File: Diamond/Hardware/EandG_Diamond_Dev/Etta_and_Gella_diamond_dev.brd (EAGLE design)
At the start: 104 x 110.1 mm, 123 parts, among them Q1 ZXMP6A13F, U1 ATSAMD21G-A, U2 3.3V, U5 OPA344, U6 ADMP401, U7 APDS-9960, Y1 32.768kHz

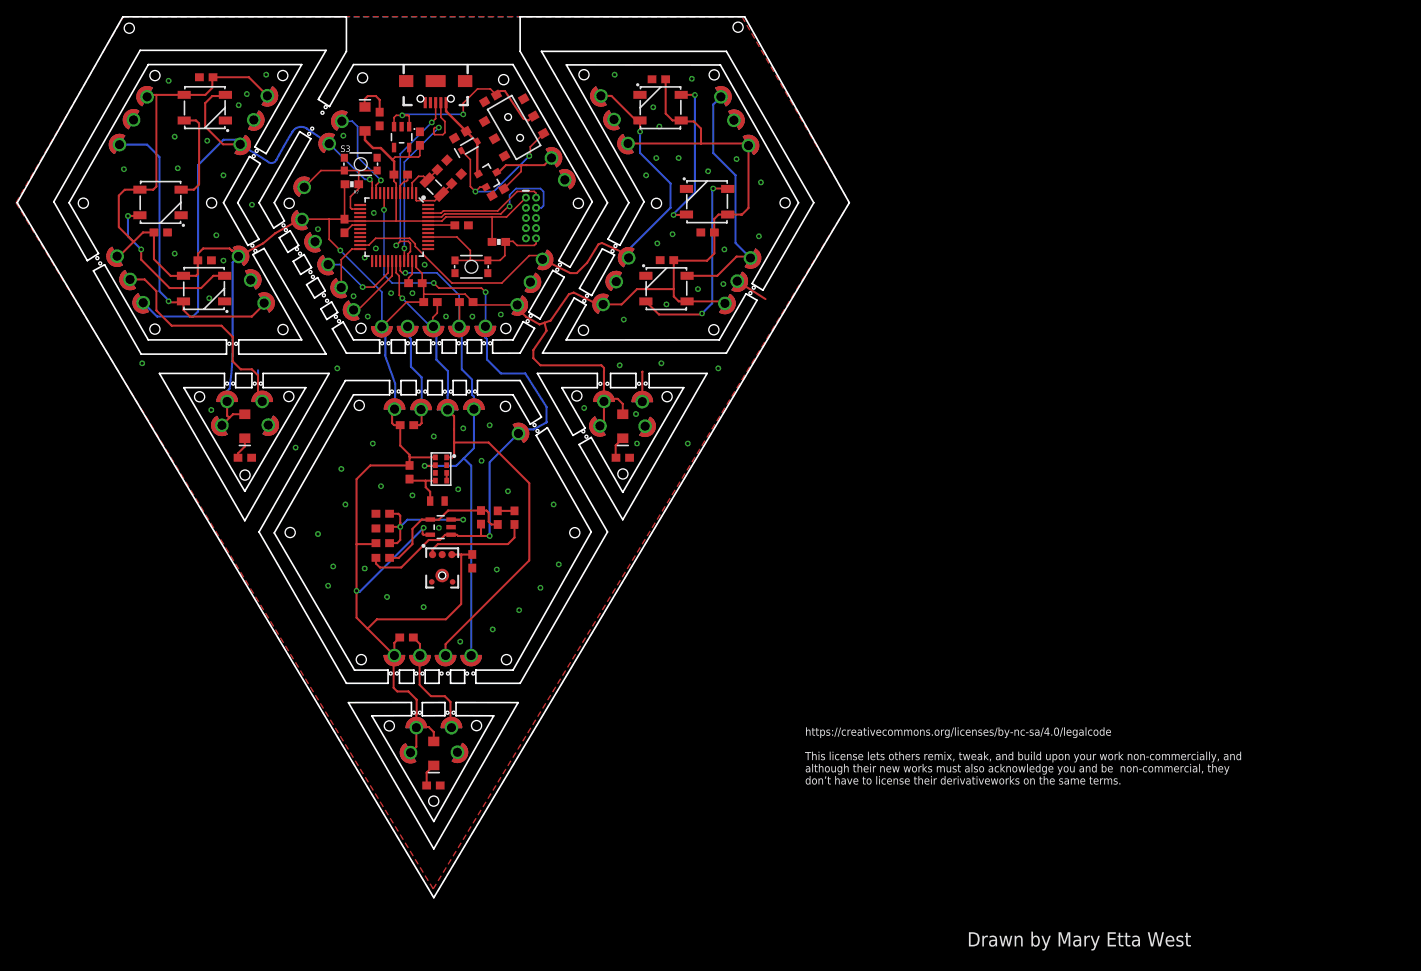
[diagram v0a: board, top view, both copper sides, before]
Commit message: Moved LEDs to D7, changed pinout on the right chevron, etc.
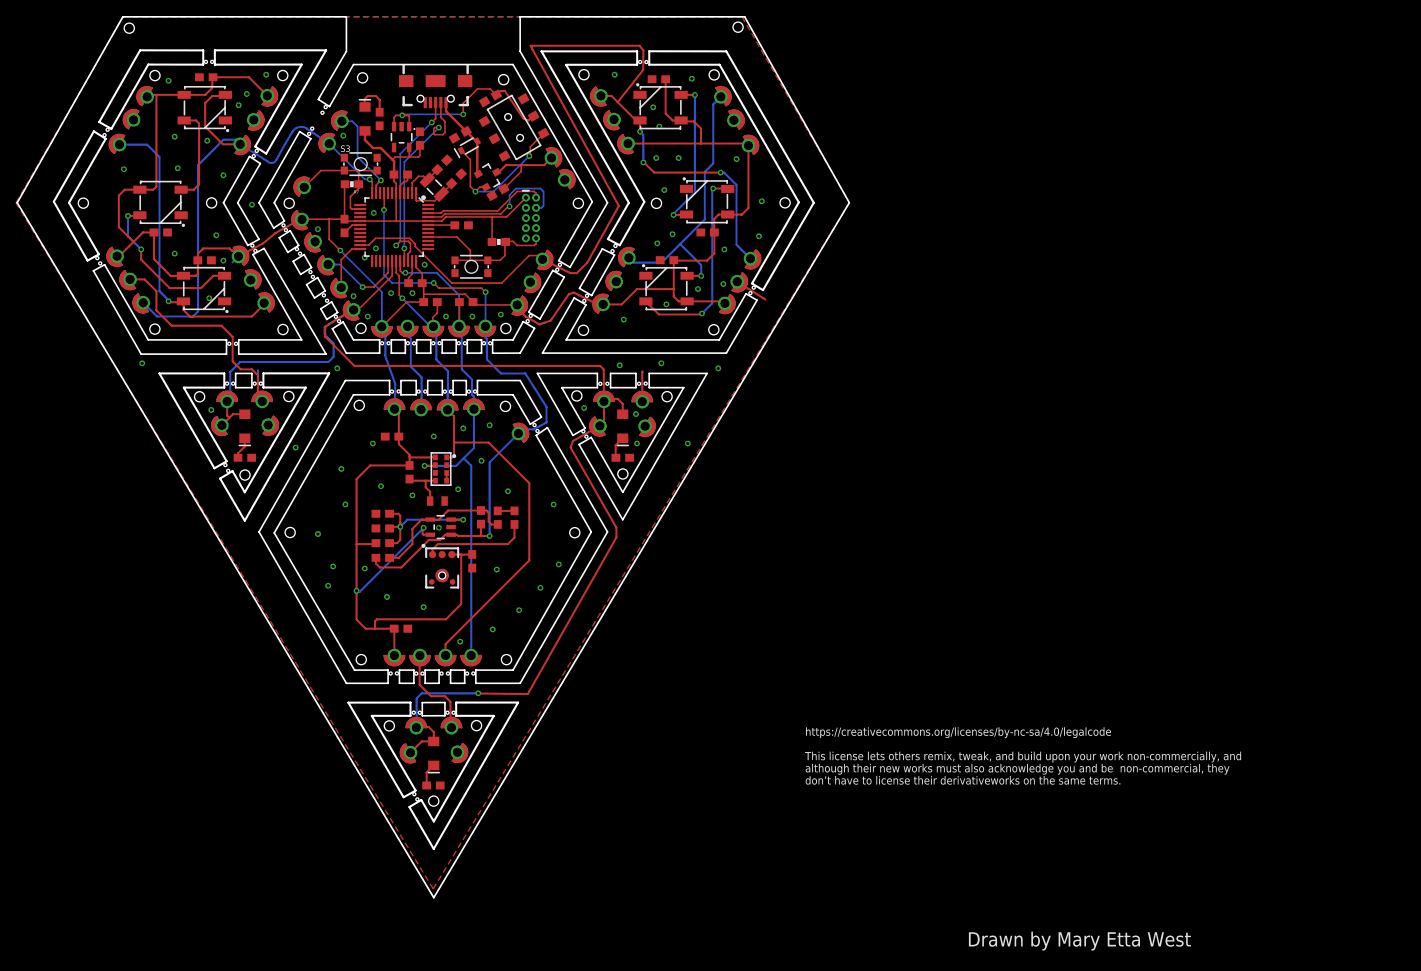
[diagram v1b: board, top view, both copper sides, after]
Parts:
- moved J42 15.2 mm to (113.4, 90.9), turned to 240 degrees
- moved J50 15.2 mm to (98.2, 91.0), turned to 60 degrees
- moved C15 2.35 mm to (68.6, 68.7), turned to 180 degrees
- moved C8 1.30 mm to (69.7, 44.7)
- moved J58 0.07 mm to (111.7, 88.0)
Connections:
- net 3.3V: no longer D1.A, D3.A, D4.A, J20.P$1, J62.P$1, J64.P$1, J68.P$1, J70.P$1, J77.P$1
- net D7: now also D1.A, D3.A, D4.A, J20.P$1, J62.P$1, J64.P$1, J68.P$1, J70.P$1, J77.P$1
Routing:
- net D7: track 8.58 -> 159.5 mm, vias 0 -> 1
- net 3.3V: track 418.4 -> 349.6 mm
- net D2: track 67.9 -> 121.2 mm, vias 1 -> 3
- net GND: track 76.1 -> 70.7 mm, vias 81 -> 80
- net DOUT: track 31.5 -> 35.0 mm, vias 0 -> 1
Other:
- outline, holes or cut-outs redrawn

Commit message: silk added to board
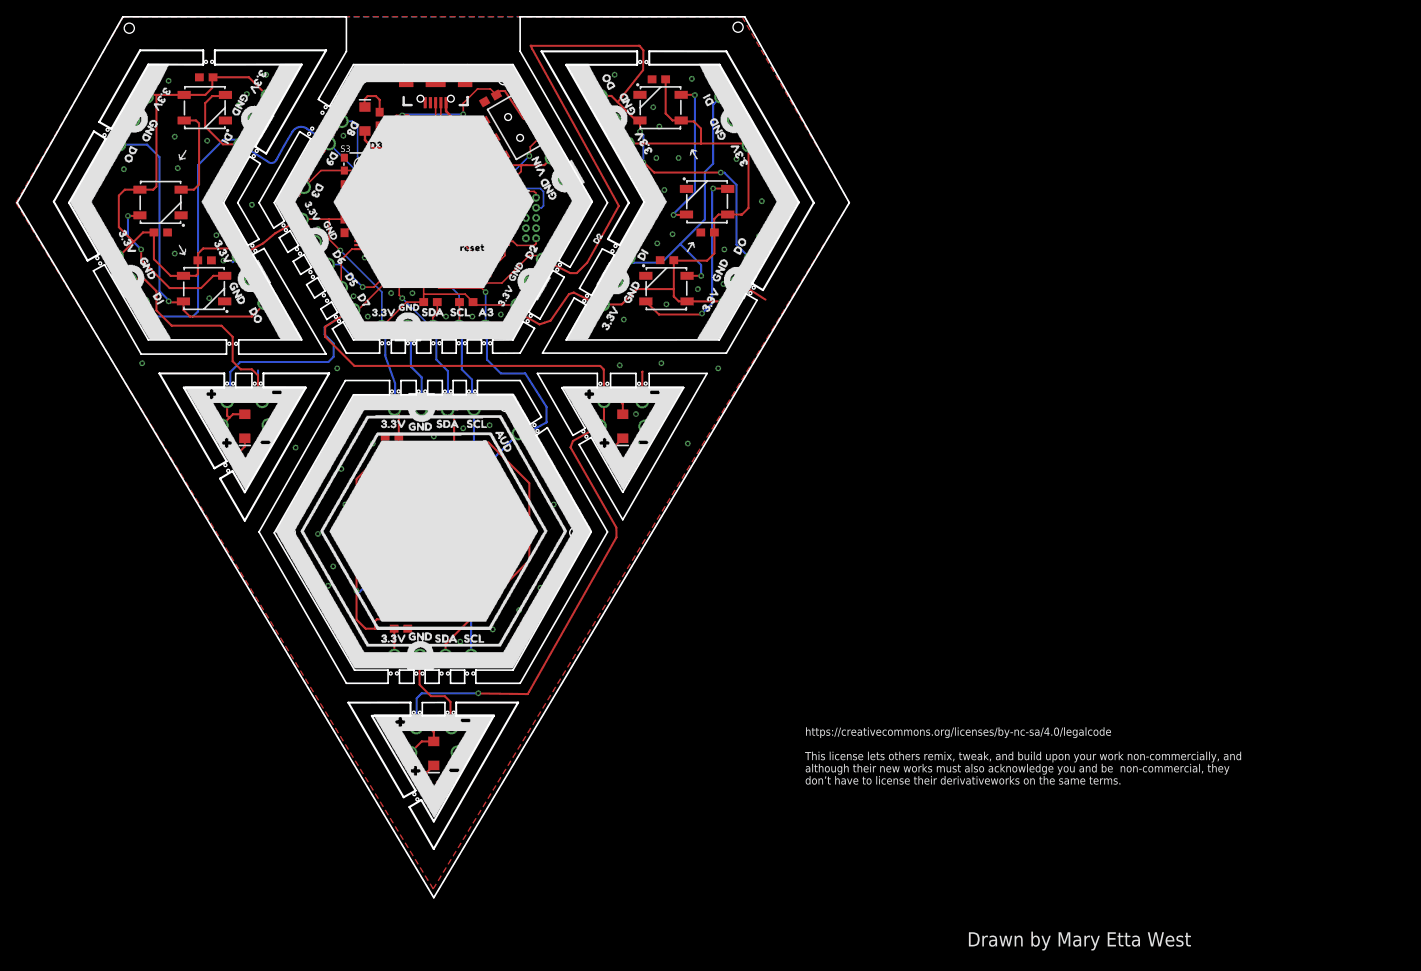
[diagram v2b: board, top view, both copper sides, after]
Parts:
- added U$2: (no value), HackModWear_V2Silk_Draft_BuzzardTop#01#jpg (1):HACKMODWEAR_V2SILK_DRAFT_BUZZARDTOP#01#JPG
- added U$3: (no value), HackModWear_V2Silk_Draft_BuzzardBottom#01#jpg (1):HACKMODWEAR_V2SILK_DRAFT_BUZZARDBOTTOM#01#JPG
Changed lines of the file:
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@@
 <layer number="27" name="tValues" color="7" fill="1" visible="no" active="yes"/>
 <layer number="28" name="bValues" color="7" fill="1" visible="no" active="yes"/>
-<layer number="29" name="tStop" color="7" fill="3" visible="no" active="yes"/>
+<layer number="29" name="tStop" color="7" fill="3" visible="yes" active="yes"/>
 <layer number="30" name="bStop" color="7" fill="6" visible="no" active="yes"/>
 <layer number="31" name="tCream" color="7" fill="4" visible="no" active="yes"/>
@@
 <attribute name="PROD_ID" value="RES-00824" x="63.5508" y="100.2284" size="1.778" layer="27" rot="R180" display="off"/>
 </element>
+<element name="U$2" library="HackModWear_V2Silk_Draft_BuzzardTop#01#jpg (1)" package="HACKMODWEAR_V2SILK_DRAFT_BUZZARDTOP#01#JPG" value="" x="73.84" y="66.02"/>
+<element name="U$3" library="HackModWear_V2Silk_Draft_BuzzardBottom#01#jpg (1)" package="HACKMODWEAR_V2SILK_DRAFT_BUZZARDBOTTOM#01#JPG" value="" x="73.59" y="66.03"/>
 </elements>
 <signals>
